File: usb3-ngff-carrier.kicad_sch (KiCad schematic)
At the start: 55 parts, among them J1 KUSBX-BS1N9-1-BL30, J2 2199119-3, J3 Jack-DC, J5 Conn_01x03_Male, J6 SIM2070-6-1-30-00-A, J8 SIM2070-6-1-30-00-A, SW1 KMR221GLFS, U1 AP62301WU7

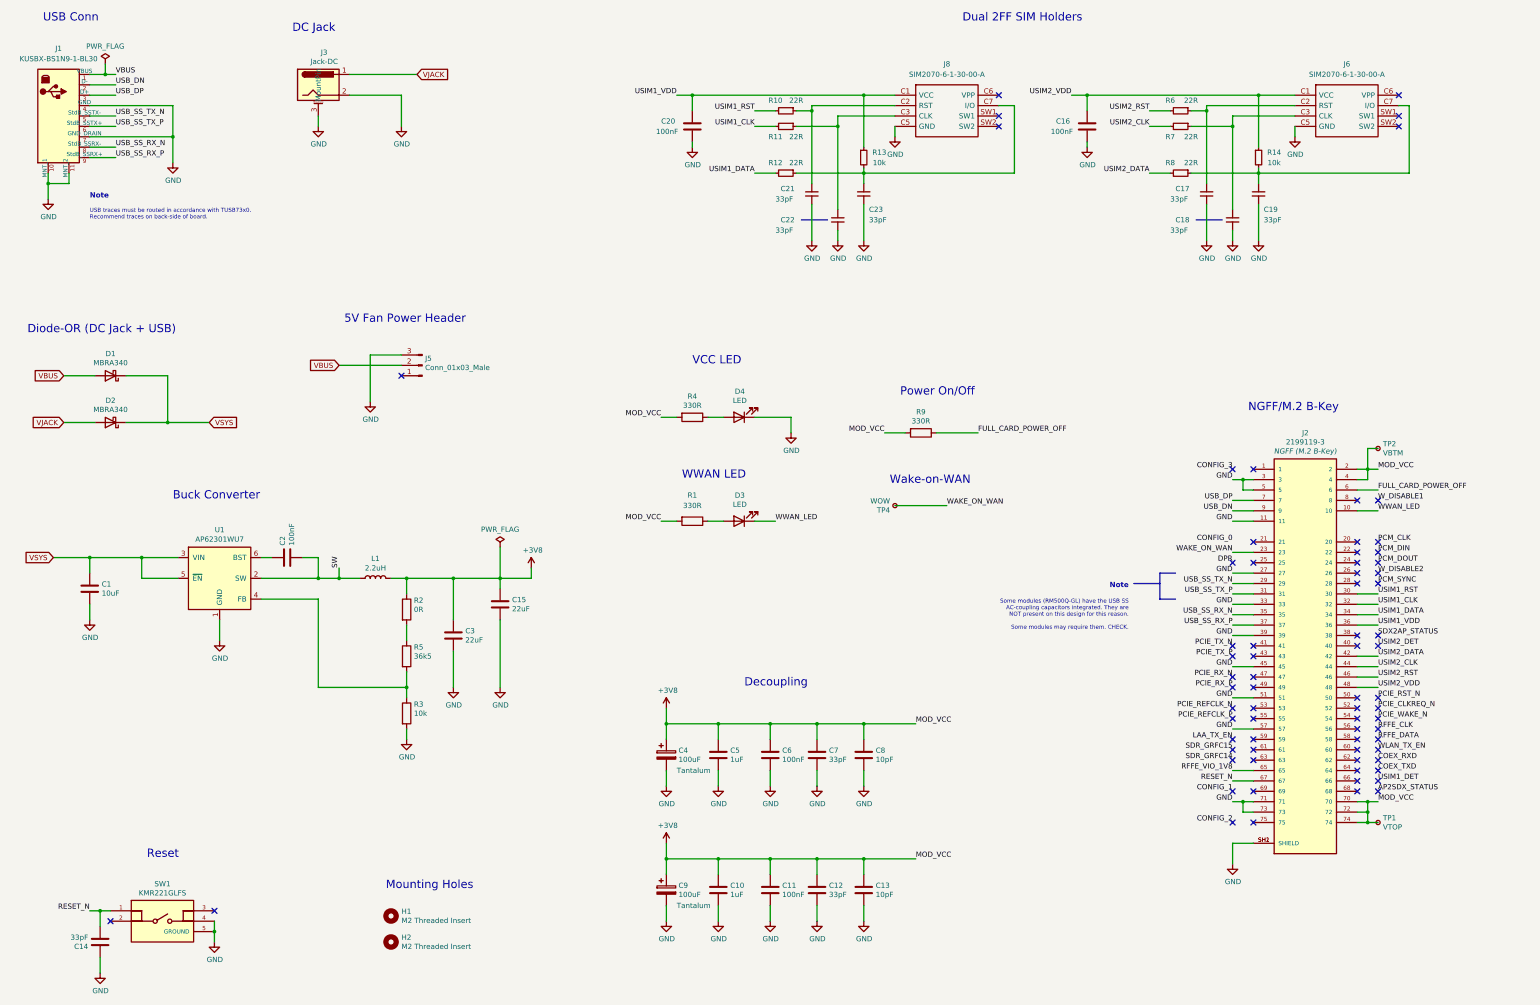
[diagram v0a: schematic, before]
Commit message: feat: properly adds sim card detection
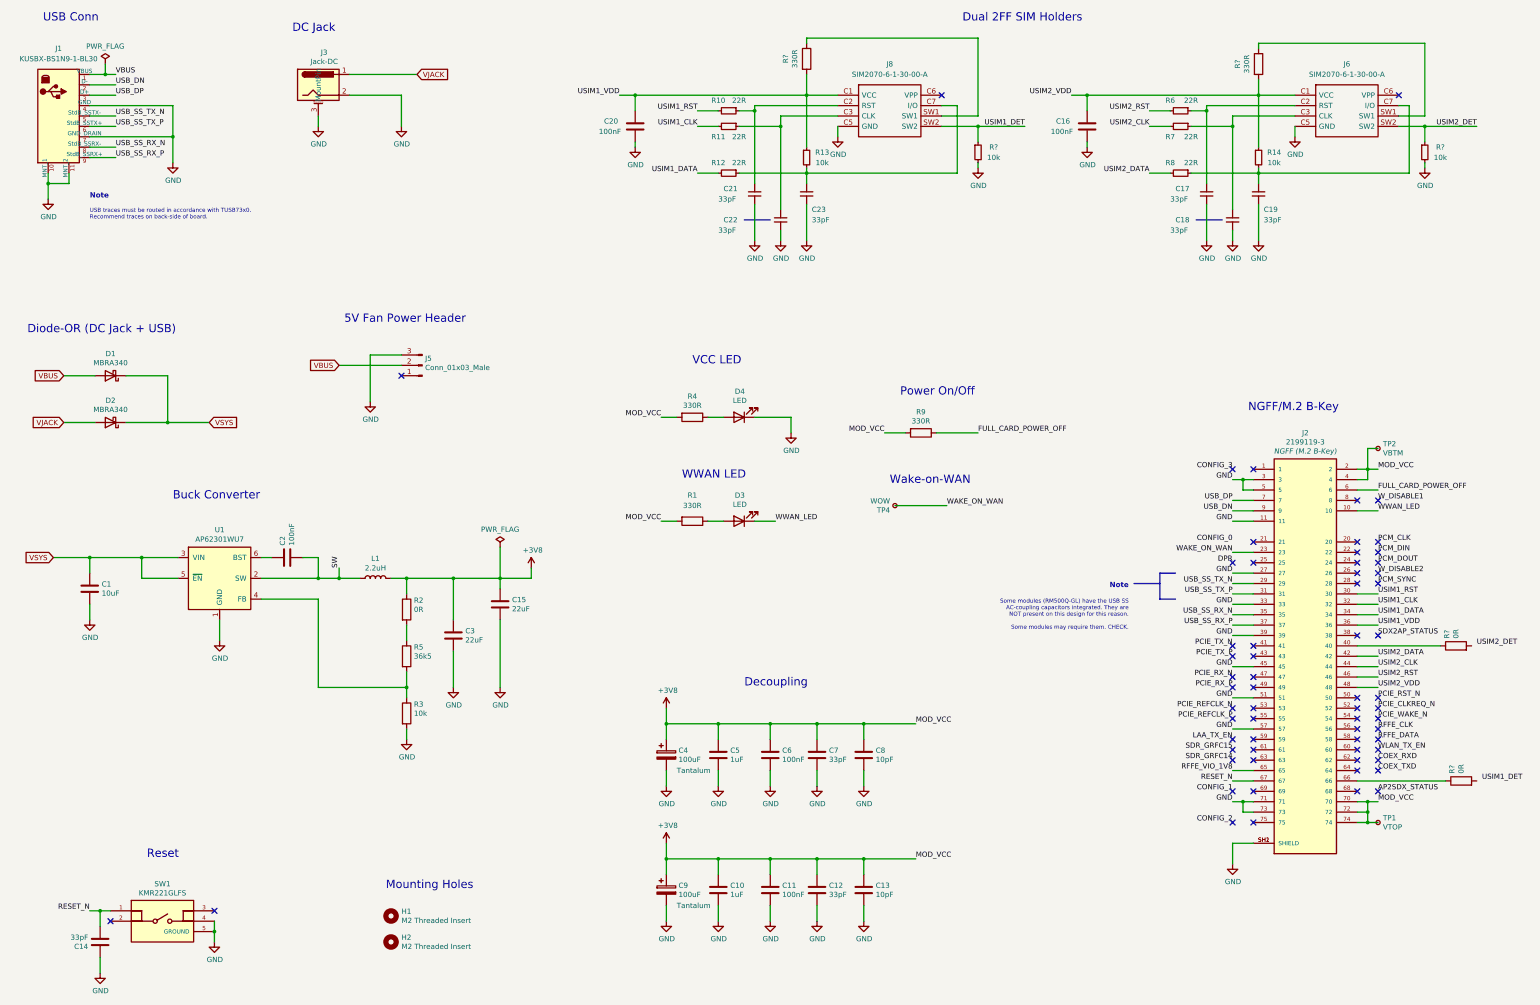
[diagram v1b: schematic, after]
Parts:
- added R? (x2): 0R, Resistor_SMD:R_0603_1608Metric, symbol Device:R
- added R? (x2): 10k, Resistor_SMD:R_0603_1608Metric, symbol Device:R_Small
- added R? (x2): 330R, Resistor_SMD:R_0603_1608Metric, symbol Device:R
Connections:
- net GND: now also R?.2, R?.2
- net USIM1_DET: now also J8.SW2, R?.1
- net USIM1_VDD: now also R?.2
- net USIM2_DET: now also J6.SW2, R?.1
- net USIM2_VDD: now also R?.2
- net at J2.40: now also R?.1
- net at J2.66: now also R?.1
- net at J8.SW1: now also R?.1
- net at J6.SW1: now also R?.1
- no-connect marks 72 -> 64
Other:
- moved on the sheet: C20, C21, C22, C23, J8, R10, R11, R12, R13

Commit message: feat: adds USB 2 capacitors pads for eventual assembly
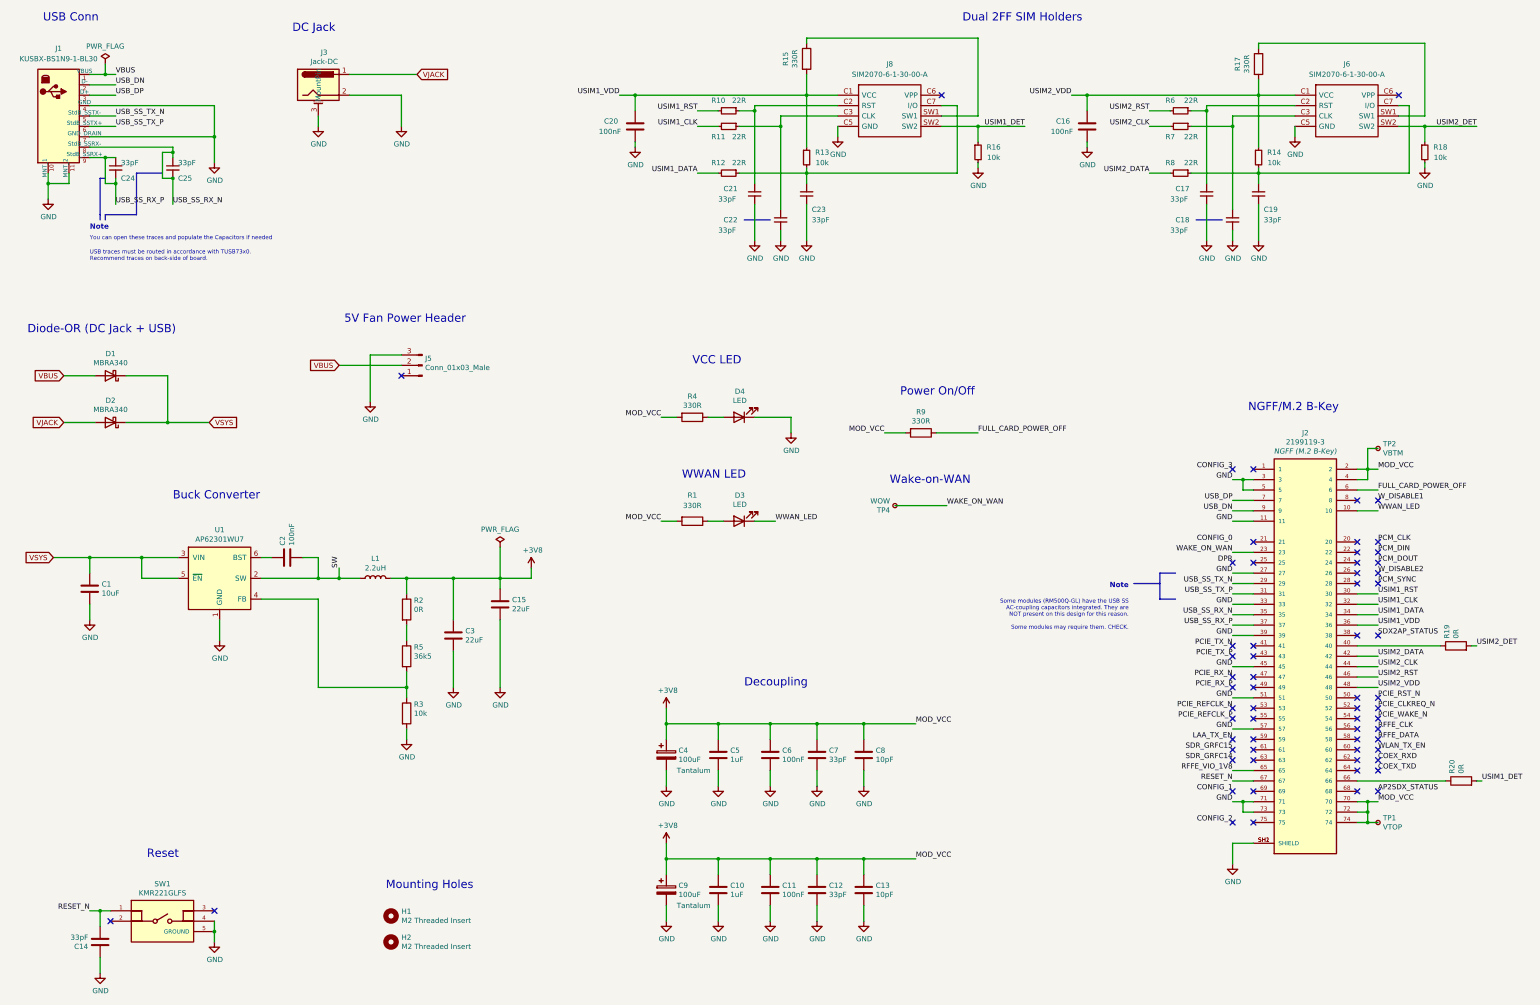
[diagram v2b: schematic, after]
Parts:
- added C24, C25: 33pF, Capacitor_SMD:C_0603_1608Metric, symbol Device:C_Small
- gave numbers to parts that had none: 6
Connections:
- net USB_SS_RX_N: now also C25.1, C25.2
- net USB_SS_RX_P: now also C24.1, C24.2
- net USIM1_DET: now also R20.2
- net USIM2_DET: now also R19.2
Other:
- note added: "You can open these traces and populate the Capacitors if needed"
